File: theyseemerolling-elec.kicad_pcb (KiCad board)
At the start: 2 copper layers, 80 x 50 mm, 88 parts, among them IC2 L6205PD, J1 Conn_Encoder1, J2 Conn_Power_In, J3 Conn_SWD_UART, J4 Conn_Mot1, J5 Conn_Mot2, J6 Conn_Encoder2, J7 CAN_conn, J8 CAN_conn, Q1 BSS138, Q2 BSS138, Q3 BSS138, Q4 BSS138, Q5 BSS138, Q6 BSS138, U1 STM32F303K8Tx, U2 LD1117S50TR_SOT223, U3 ACS711xLCTR-12AB, U4 ACS711xLCTR-12AB, U5 74HC00, U6 LD1117S33TR_SOT223, U7 MCP2551-I-SN, U8 AT25SF041

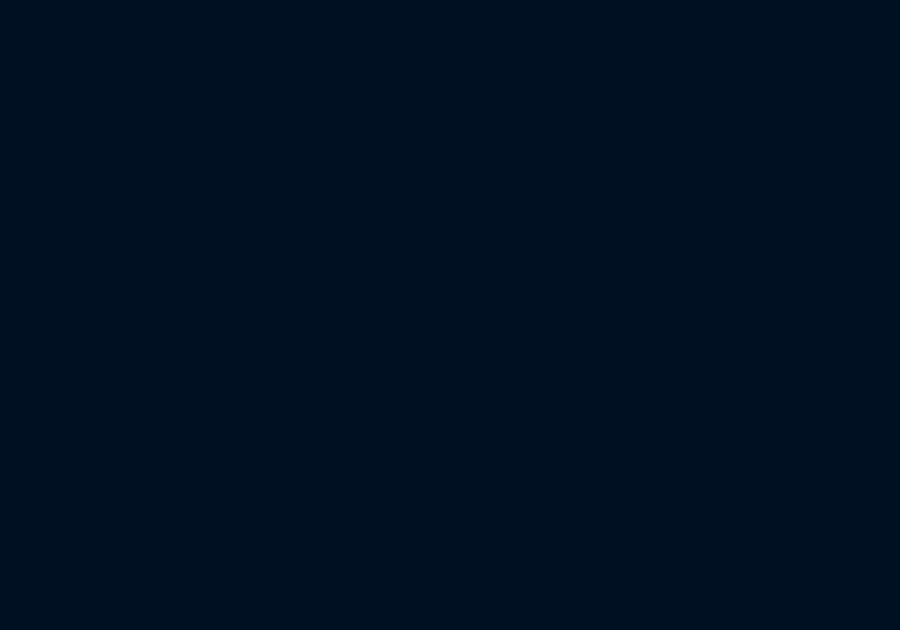
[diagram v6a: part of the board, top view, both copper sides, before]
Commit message: footprint 0805
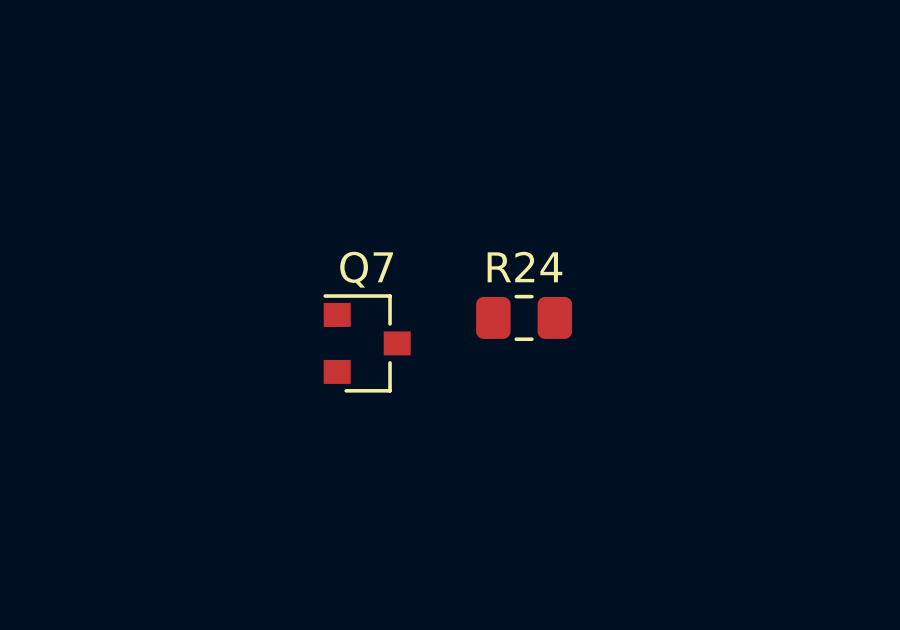
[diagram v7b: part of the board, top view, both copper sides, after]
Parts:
- added Q7: BSS138, Package_TO_SOT_SMD:SOT-23, F.Cu at (123.2, 26.5)
- added R24: R, Resistor_SMD:R_0805_2012Metric_Pad1.15x1.40mm_HandSolder, F.Cu at (128.4, 25.6)
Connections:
- R23 pad 1: Net-(Q6-Pad3) -> /f3/CAN_TX
- R23 pad 2: +5V -> +3V3
- U7 pad 1: /f3/CAN_TX -> Net-(Q7-Pad3)
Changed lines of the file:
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@@
     (tracks 598)
     (zones 0)
-    (modules 88)
-    (nets 69)
+    (modules 90)
+    (nets 70)
   )
   (page A4)
@@
   (net 67 "Net-(Q4-Pad2)")
   (net 68 "Net-(Q5-Pad2)")
+  (net 69 "Net-(Q7-Pad3)")
   (net_class Default "This is the default net class."
     (clearance 0.2)
@@
     (add_net "Net-(Q5-Pad2)")
     (add_net "Net-(Q6-Pad3)")
+    (add_net "Net-(Q7-Pad3)")
     (add_net "Net-(R1-Pad1)")
     (add_net "Net-(R13-Pad2)")
@@
     (add_net VCC)
   )
+  (module Package_TO_SOT_SMD:SOT-23 (layer F.Cu)
+    (at 123.155952 26.4575)
+    (descr "SOT-23, Standard")
+    (tags SOT-23)
+    (attr smd)
+    (fp_text reference Q7 (at 0 -2.5) (layer F.SilkS)
+      (effects (font (size 1 1) (thickness 0.15)))
+    )
+    (fp_text value BSS138 (at 0 2.5) (layer F.Fab)
+      (effects (font (size 1 1) (thickness 0.15)))
+    )
+    (fp_text user %R (at 0 0 90) (layer F.Fab)
+      (effects (font (size 0.5 0.5) (thickness 0.075)))
+    )
+    (fp_line (start -0.7 -0.95) (end -0.7 1.5) (layer F.Fab) (width 0.1))
+    (fp_line (start -0.15 -1.52) (end 0.7 -1.52) (layer F.Fab) (width 0.1))
+    (fp_line (start -0.7 -0.95) (end -0.15 -1.52) (layer F.Fab) (width 0.1))
+    (fp_line (start 0.7 -1.52) (end 0.7 1.52) (layer F.Fab) (width 0.1))
+    (fp_line (start -0.7 1.52) (end 0.7 1.52) (layer F.Fab) (width 0.1))
+    (fp_line (start 0.76 1.58) (end 0.76 0.65) (layer F.SilkS) (width 0.12))
+    (fp_line (start 0.76 -1.58) (end 0.76 -0.65) (layer F.SilkS) (width 0.12))
+    (fp_line (start -1.7 -1.75) (end 1.7 -1.75) (layer F.CrtYd) (width 0.05))
+    (fp_line (start 1.7 -1.75) (end 1.7 1.75) (layer F.CrtYd) (width 0.05))
+    (fp_line (start 1.7 1.75) (end -1.7 1.75) (layer F.CrtYd) (width 0.05))
+    (fp_line (start -1.7 1.75) (end -1.7 -1.75) (layer F.CrtYd) (width 0.05))
+    (fp_line (start 0.76 -1.58) (end -1.4 -1.58) (layer F.SilkS) (width 0.12))
+    (fp_line (start 0.76 1.58) (end -0.7 1.58) (layer F.SilkS) (width 0.12))
+    (pad 1 smd rect (at -1 -0.95) (size 0.9 0.8) (layers F.Cu F.Paste F.Mask)
+      (net 19 +3V3))
+    (pad 2 smd rect (at -1 0.95) (size 0.9 0.8) (layers F.Cu F.Paste F.Mask)
+      (net 48 /f3/CAN_TX))
+    (pad 3 smd rect (at 1 0) (size 0.9 0.8) (layers F.Cu F.Paste F.Mask)
+      (net 69 "Net-(Q7-Pad3)"))
+    (model ${KISYS3DMOD}/Package_TO_SOT_SMD.3dshapes/SOT-23.wrl
+      (at (xyz 0 0 0))
+      (scale (xyz 1 1 1))
+      (rotate (xyz 0 0 0))
+    )
+  )
+  (module Resistor_SMD:R_0805_2012Metric_Pad1.15x1.40mm_HandSolder (layer F.Cu)
+    (at 128.385001 25.6075)
+    (descr "Resistor SMD 0805 (2012 Metric), square (rectangular) end terminal, IPC_7351 nominal with elongated pad for handsoldering. (Body size source: https://docs.google.com/spreadsheets/d/1BsfQQcO9C6DZCsRaXUlFlo91Tg2WpOkGARC1WS5S8t0/edit?usp=sharing), generated with kicad-footprint-generator")
+    (tags "resistor handsolder")
+    (attr smd)
+    (fp_text reference R24 (at 0 -1.65) (layer F.SilkS)
+      (effects (font (size 1 1) (thickness 0.15)))
+    )
+    (fp_text value R (at 0 1.65) (layer F.Fab)
+      (effects (font (size 1 1) (thickness 0.15)))
+    )
+    (fp_line (start -1 0.6) (end -1 -0.6) (layer F.Fab) (width 0.1))
+    (fp_line (start -1 -0.6) (end 1 -0.6) (layer F.Fab) (width 0.1))
+    (fp_line (start 1 -0.6) (end 1 0.6) (layer F.Fab) (width 0.1))
+    (fp_line (start 1 0.6) (end -1 0.6) (layer F.Fab) (width 0.1))
+    (fp_line (start -0.261252 -0.71) (end 0.261252 -0.71) (layer F.SilkS) (width 0.12))
+    (fp_line (start -0.261252 0.71) (end 0.261252 0.71) (layer F.SilkS) (width 0.12))
+    (fp_line (start -1.85 0.95) (end -1.85 -0.95) (layer F.CrtYd) (width 0.05))
+    (fp_line (start -1.85 -0.95) (end 1.85 -0.95) (layer F.CrtYd) (width 0.05))
+    (fp_line (start 1.85 -0.95) (end 1.85 0.95) (layer F.CrtYd) (width 0.05))
+    (fp_line (start 1.85 0.95) (end -1.85 0.95) (layer F.CrtYd) (width 0.05))
+    (fp_text user %R (at 0 0) (layer F.Fab)
+      (effects (font (size 0.5 0.5) (thickness 0.08)))
+    )
+    (pad 1 smd roundrect (at -1.025 0) (size 1.15 1.4) (layers F.Cu F.Paste F.Mask) (roundrect_rratio 0.217391)
+      (net 64 "Net-(Q6-Pad3)"))
+    (pad 2 smd roundrect (at 1.025 0) (size 1.15 1.4) (layers F.Cu F.Paste F.Mask) (roundrect_rratio 0.217391)
+      (net 22 +5V))
+    (model ${KISYS3DMOD}/Resistor_SMD.3dshapes/R_0805_2012Metric.wrl
+      (at (xyz 0 0 0))
+      (scale (xyz 1 1 1))
+      (rotate (xyz 0 0 0))
+    )
+  )
   (module Resistor_SMD:R_0805_2012Metric_Pad1.33x1.40mm_HandSolder (layer F.Cu)
     (at 104 36)
@@
     )
     (pad 1 smd rect (at -0.9375 0) (size 1.325 1.4) (layers F.Cu F.Paste F.Mask)
-      (net 64 "Net-(Q6-Pad3)"))
+      (net 48 /f3/CAN_TX))
     (pad 2 smd rect (at 0.9375 0) (size 1.325 1.4) (layers F.Cu F.Paste F.Mask)
-      (net 22 +5V))
+      (net 19 +3V3))
     (model ${KISYS3DMOD}/Resistor_SMD.3dshapes/R_0805_2012Metric.wrl
       (at (xyz 0 0 0))
@@
     (fp_line (start -2.075 -2.525) (end -3.475 -2.525) (layer F.SilkS) (width 0.15))
     (pad 1 smd rect (at -2.7 -1.905 90) (size 1.55 0.6) (layers F.Cu F.Paste F.Mask)
-      (net 48 /f3/CAN_TX))
+      (net 69 "Net-(Q7-Pad3)"))
     (pad 2 smd rect (at -2.7 -0.635 90) (size 1.55 0.6) (layers F.Cu F.Paste F.Mask)
       (net 7 GND))

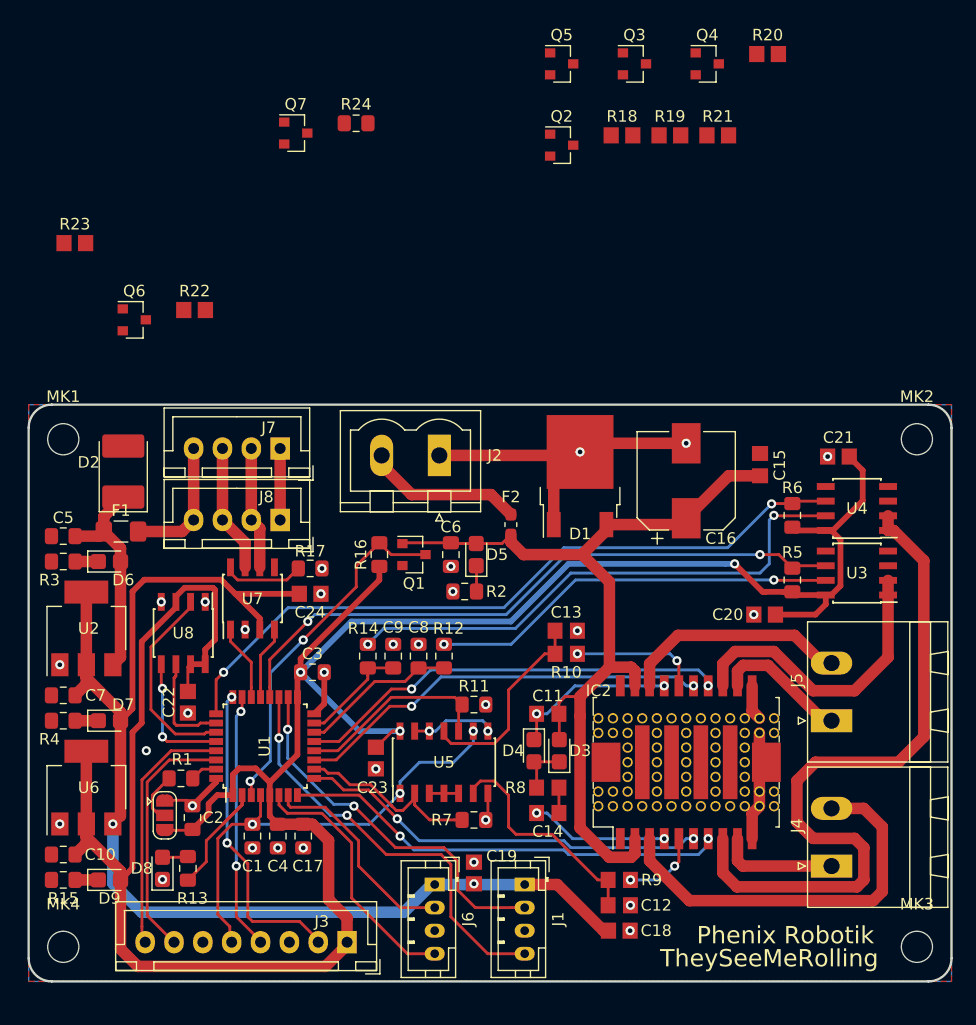
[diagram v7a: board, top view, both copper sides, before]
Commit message: Start to put components on both sides
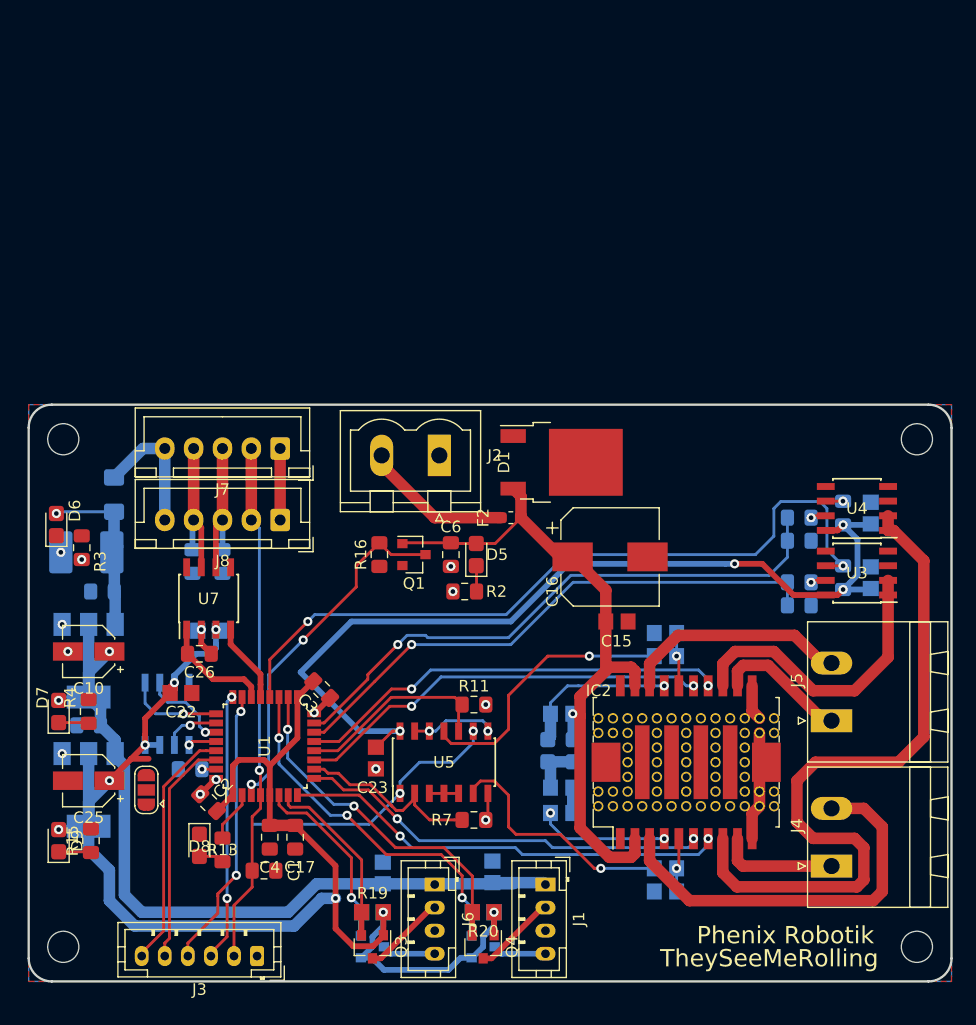
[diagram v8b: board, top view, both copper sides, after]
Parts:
- removed Q6, Q7: BSS138, Package_TO_SOT_SMD:SOT-23
- removed R17: 47kR, Resistor_SMD:R_0805_2012Metric_Pad1.15x1.40mm_HandSolder
- removed R22, R23: R, Resistor_SMD:R_0805_2012Metric_Pad1.33x1.40mm_HandSolder
- removed R24: R, Resistor_SMD:R_0805_2012Metric_Pad1.15x1.40mm_HandSolder
- added C25: 10u, Capacitor_SMD:CP_Elec_4x5.4, F.Cu at (105.2, 82.6)
- added C26: 100p, Capacitor_SMD:C_0805_2012Metric_Pad1.15x1.40mm_HandSolder, F.Cu at (114.8, 71.6)
- added C27: 100p, Capacitor_SMD:C_0805_2012Metric_Pad1.15x1.40mm_HandSolder, B.Cu at (114.2, 63.6)
- added C28: 100p, Capacitor_SMD:C_0805_2012Metric_Pad1.15x1.40mm_HandSolder, B.Cu at (116.8, 63.6)
- C10: value C -> 10u; footprint Capacitor_SMD:C_0805_2012Metric_Pad1.15x1.40mm_HandSolder -> Capacitor_SMD:CP_Elec_4x5.4
- C11, C14, C18, C19, C20, C21, C24, D2, D3, D4, Q2, Q5, R1, R10, R12, R14, R18, R21, R5, R6, R8, R9, U2, U6, U8: moved to B.Cu
- C12, C13: value 68n -> 5.6n; moved to B.Cu
- C5, C7: value C -> 100n; moved to B.Cu
- C8, C9: value C -> 1n; moved to B.Cu
- F1: value Polyfuse -> Polyfuse 2A; moved to B.Cu
- F2: value Fuse -> 5A
- J3: footprint Connector_JST:JST_XH_B08B-XH-A_1x08_P2.50mm_Vertical -> Connector_JST:JST_PH_B6B-PH-K_1x06_P2.00mm_Vertical
- J7, J8: footprint Connector_JST:JST_XH_B04B-XH-A_1x04_P2.50mm_Vertical -> Connector_JST:JST_XH_B05B-XH-A_1x05_P2.50mm_Vertical
- U7: value MCP2551-I-SN -> TCAN332
- moved Q3 79.8 mm to (129.8, 97.0), turned to 270 degrees
- moved Q4 79.0 mm to (139.4, 97.0), turned to 270 degrees
- moved R20 78.4 mm to (139.4, 94.0), turned to 180 degrees
- moved Q5 76.8 mm to (139.4, 97.0)
- moved R19 72.1 mm to (129.8, 94.0)
- moved Q2 71.4 mm to (129.8, 97.0)
- moved R18 70.7 mm to (129.8, 94.0), turned to 180 degrees
- moved R21 70.3 mm to (139.4, 94.0)
- moved R14 39.3 mm to (166.8, 59.8), turned to 180 degrees
- moved C9 36.6 mm to (166.8, 61.8), turned to 0 degrees
- moved C8 33.3 mm to (166.8, 67.4), turned to 0 degrees
- moved R12 31.5 mm to (166.8, 65.4), turned to 180 degrees
- moved C15 18.4 mm to (151.0, 68.8), turned to 0 degrees
- moved C10 17.7 mm to (105.2, 71.4)
- moved C18 12.1 mm to (140.2, 90.5), turned to 90 degrees
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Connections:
- C1 pad 2: /f3/nrst -> /CAN/NRST
- C10 pad 1: +3V3 -> +5V
- C12 pad 1: /DualDCDriver/EN_A -> Net-(C12-Pad1)
- C13 pad 1: /DualDCDriver/EN_B -> Net-(C13-Pad1)
- C24 pad 1: +5V -> +3V3
- IC2 pad 16: Net-(IC2-Pad16) -> Net-(C13-Pad1)
- IC2 pad 5: Net-(IC2-Pad5) -> Net-(C12-Pad1)
- J3 pad 1: +3V3 -> GND
- J3 pad 2: /f3/TCK -> /CAN/NRST
- J3 pad 3: GND -> /f3/TCK
- J3 pad 5: /f3/nrst -> /f3/RX_1
- J3 pad 6: Net-(J3-Pad6) -> /f3/TX_1
- J7 pad 2: Net-(J7-Pad2) -> /CAN/NRST
- J7 pad 3: Net-(J7-Pad3) -> Net-(C28-Pad1)
- J7 pad 4: /CAN/+7V_CAN -> Net-(C27-Pad2)
- J8 pad 2: Net-(J7-Pad2) -> /CAN/NRST
- J8 pad 3: Net-(J7-Pad3) -> Net-(C28-Pad1)
- J8 pad 4: /CAN/+7V_CAN -> Net-(C27-Pad2)
- R10 pad 1: Net-(IC2-Pad16) -> Net-(C13-Pad1)
- R9 pad 1: Net-(IC2-Pad5) -> Net-(C12-Pad1)
- U1 pad 20: /DualDCDriver/Sense_B_Fault -> Net-(U1-Pad20)
- U1 pad 25: /DualDCDriver/Sense_A_Fault -> Net-(U1-Pad25)
- U1 pad 4: /f3/nrst -> /CAN/NRST
- U5 pad 1: /f3/nrst -> /CAN/NRST
- U5 pad 9: /f3/nrst -> /CAN/NRST
- U7 pad 1: Net-(Q7-Pad3) -> /f3/CAN_TX
- U7 pad 3: +5V -> +3V3
- U7 pad 4: Net-(Q6-Pad3) -> /f3/CAN_RX
- U7 pad 6: Net-(J7-Pad2) -> Net-(C28-Pad1)
- U7 pad 7: Net-(J7-Pad3) -> Net-(C27-Pad2)
- U8 pad 1: GND -> Net-(U1-Pad25)
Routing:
- net /CAN/NRST: track 0.00 -> 69.1 mm, vias 0 -> 3
- net /DualDCDriver/Sense_A_Fault: track 62.2 -> 1.50 mm, vias 2 -> 1
- net /DualDCDriver/Sense_A: track 46.6 -> 1.34 mm, vias 2 -> 1
- net /f3/Sense_A_Filtered: track 9.40 -> 50.8 mm, vias 0 -> 1
- net /f3/nrst: track 39.4 -> 0.00 mm, vias 3 -> 0
- net /f3/Sense_B_Filtered: track 13.6 -> 48.4 mm, vias 0 -> 1
- net +5V: track 106.5 -> 72.1 mm
- net /DualDCDriver/Sense_B: track 35.5 -> 1.34 mm, vias 2 -> 1
- net GND: track 60.6 -> 28.3 mm, vias 30 -> 14
- net /f3/Encoder_1_B: track 36.6 -> 4.65 mm, vias 2 -> 0
- net Net-(Q5-Pad2): track 0.00 -> 31.3 mm, vias 0 -> 3
- net Net-(Q4-Pad2): track 0.00 -> 30.7 mm, vias 0 -> 2
- net /f3/Encoder_1_A: track 32.7 -> 7.22 mm, vias 2 -> 0
- net +3V3: track 226.3 -> 205.7 mm, vias 3 -> 12
- net VCC: track 77.4 -> 59.1 mm, vias 0 -> 1
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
